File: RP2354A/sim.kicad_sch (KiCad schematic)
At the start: 10 parts

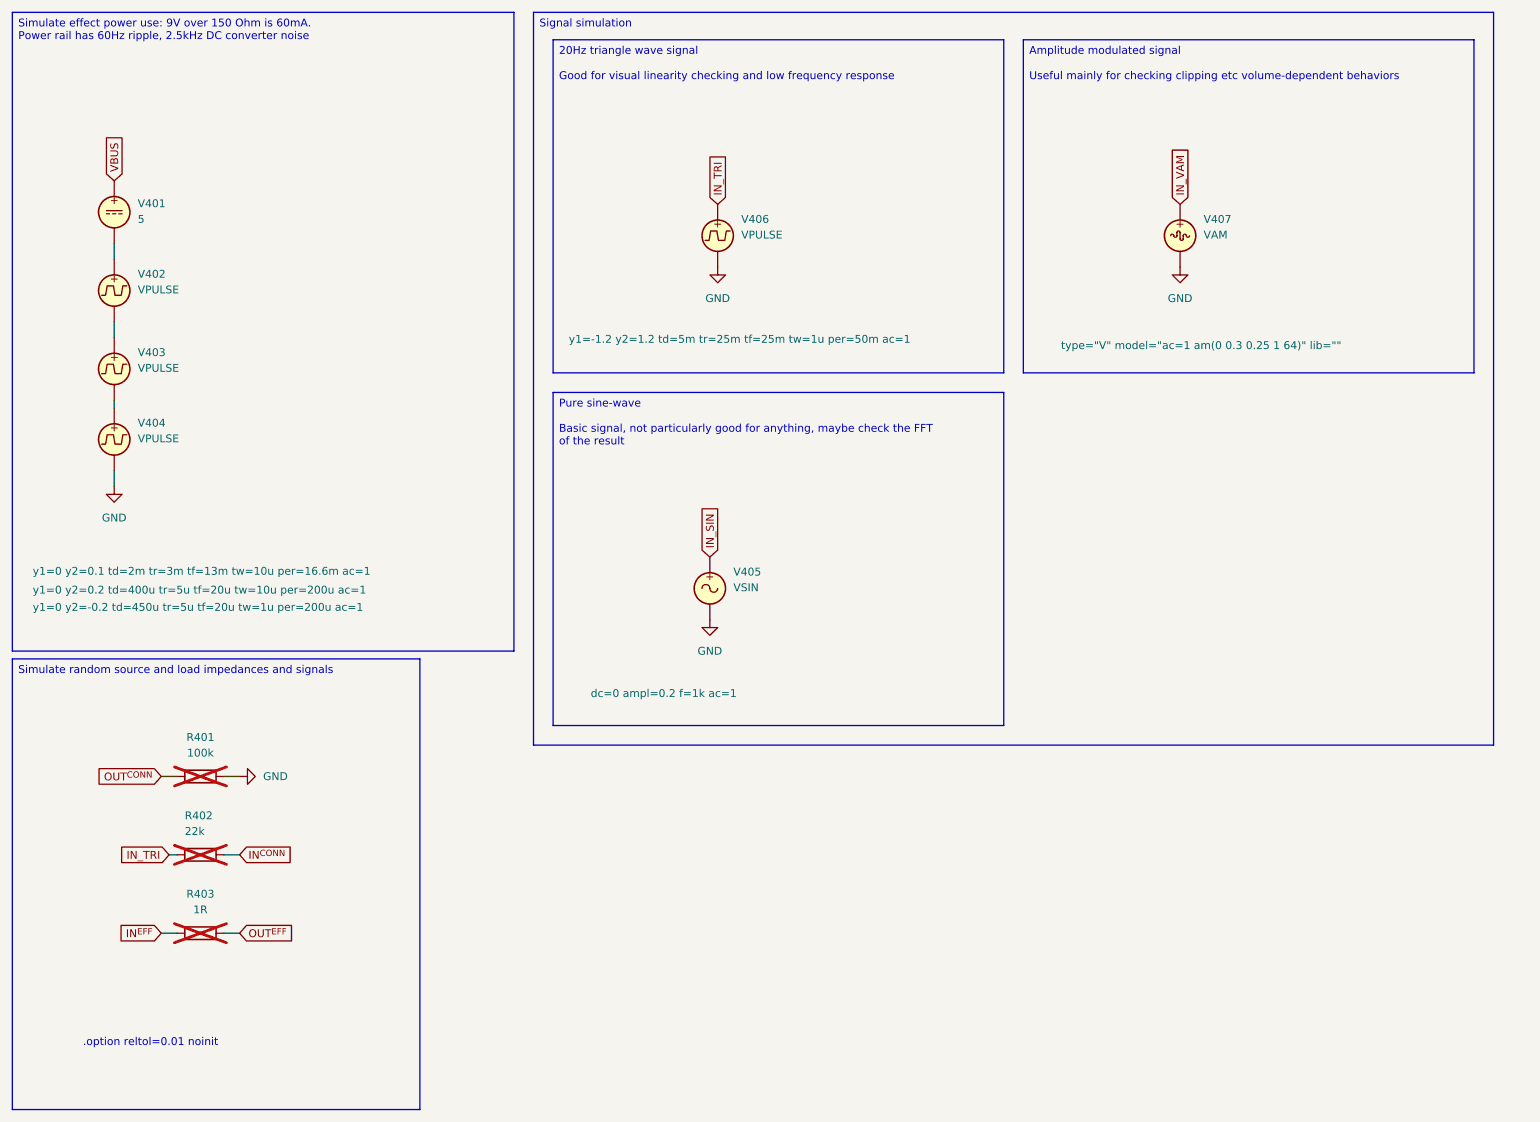
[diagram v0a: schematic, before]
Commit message: Switch the MMBF5103 JFET over to a OPA365 op amp
This is a long time coming, but it was triggered by jlcpcb not stocking
the MMBF5103, and all the alternatives looked worse.  So I guess sanity
has to prevail, and I should use an opamp rather than a discrete JFET
input stage.

I looked at the J201 - which I have tested and works, but has a
potentially very low V_{GSOFF} that will cause clipping.  And the
MMBFJ309L looked good in simulation and had better parameter values, but
I've never tested it, so it seemed a bit risky particularly since the
intended market seems to be for much higher frequency circuits.

I even looked at the JFE150, which is another silly-expensive thing sold
to audio markets.  I guess that tracks.

In the end, a plain simple opamp is definitely the sane choice.

To rebias the incoming signal, this uses the MICBIAS from the TAC5112,
which is typically 2.75V (but can be programmed to 2.5V or turned off
entirely etc).  It's there, it's almost what it is meant for, so let's
use it.

The OPA365 looks fine, and does rail-to-rail input and output and can do
single supplies down to 2.2V, but rather than put even more on the 3.3V
rail (and limiting the voltage swing), this just uses the 5V USB VBUS
power supply.

This does have some minimal caps for filtering (replacing the old +VA
supply to the JFET) but the OPA365 also claims good PSRR.

This all does seem like the right thing to do, but I'm still a bit sad
since the discrete JFET was just more interesting.

Signed-off-by: Linus Torvalds <torvalds@linux-foundation.org>
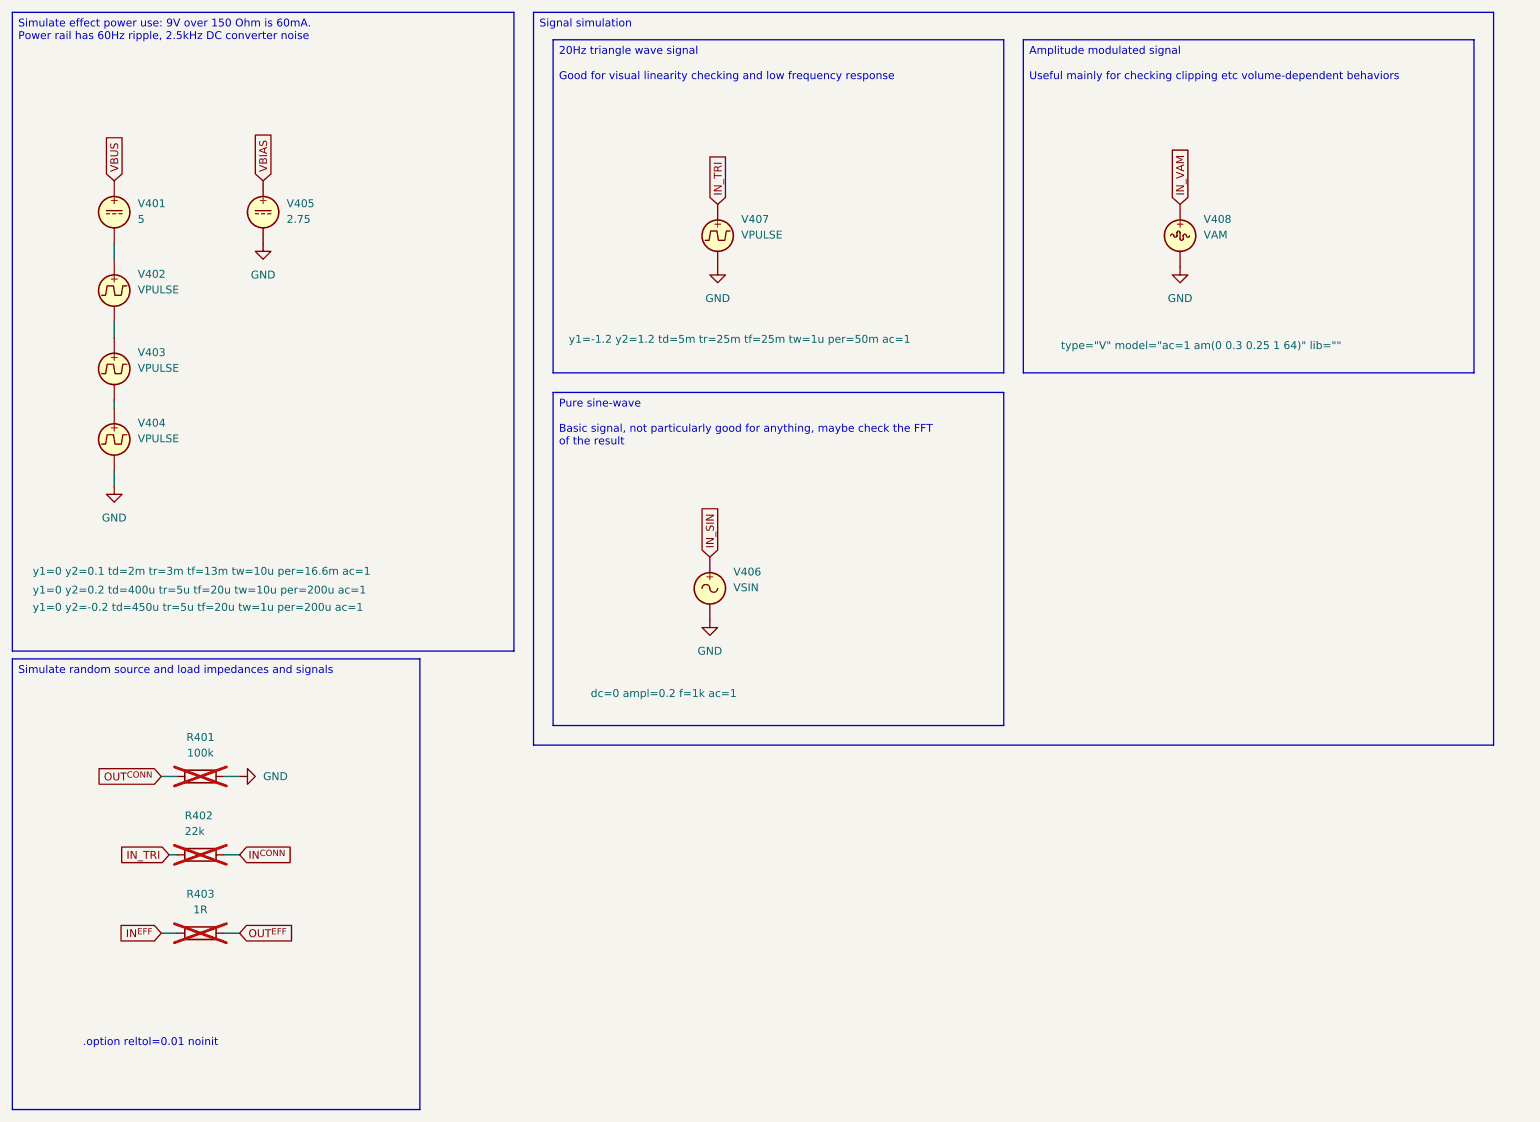
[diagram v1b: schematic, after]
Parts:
- added V405: 2.75, symbol Simulation_SPICE:VDC
- renumbered V405 to V406, V406 to V407, V407 to V408
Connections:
- net GND: now also V405.2
- new net VBIAS: V405.1
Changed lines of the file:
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@@
+		)
+	)
+	(global_label "VBIAS"
+		(shape input)
+		(at 54.61 41.91 90)
+		(fields_autoplaced yes)
+		(effects
+			(font
+				(size 1.27 1.27)
+			)
+			(justify left)
+		)
+		(property "Intersheetrefs" "${INTERSHEET_REFS}"
+			(at 54.61 33.6633 90)
+			(effects
+				(font
+					(size 1.27 1.27)
+				)
+				(justify left)
+				(hide yes)
+			)
 		)
 	)
@@
 		(dnp no)
 		(fields_autoplaced yes)
-		(property "Reference" "#PWR0303"
+		(property "Reference" "#PWR0404"
 			(at 127 119.38 0)
 			(effects
@@
 			(project "Stomp"
 				(path "/9e337e0b-885b-4d2b-99a2-62cdd082c615/a1084b87-85fd-4b63-8fe4-8749c999d338"
-					(reference "#PWR0303")
+					(reference "#PWR0404")
 					(unit 1)
 				)
@@
 		(on_board no)
 		(dnp no)
-		(property "Reference" "V405"
+		(property "Reference" "V406"
 			(at 130.81 105.2801 0)
 			(effects
@@
 			(project "Stomp"
 				(path "/9e337e0b-885b-4d2b-99a2-62cdd082c615/a1084b87-85fd-4b63-8fe4-8749c999d338"
-					(reference "V405")
+					(reference "V406")
 					(unit 1)
 				)
@@
 		(on_board no)
 		(dnp no)
-		(property "Reference" "V407"
+		(property "Reference" "V408"
 			(at 207.01 48.1301 0)
 			(effects
@@
 			(project "Stomp"
 				(path "/9e337e0b-885b-4d2b-99a2-62cdd082c615/a1084b87-85fd-4b63-8fe4-8749c999d338"
-					(reference "V407")
+					(reference "V408")
 					(unit 1)
 				)
@@
 				(path "/9e337e0b-885b-4d2b-99a2-62cdd082c615/a1084b87-85fd-4b63-8fe4-8749c999d338"
 					(reference "R401")
+					(unit 1)
+				)
+			)
+		)
+	)
+	(symbol
+		(lib_id "Simulation_SPICE:VDC")
+		(at 54.61 46.99 0)
+		(unit 1)
+		(exclude_from_sim no)
+		(in_bom no)
+		(on_board no)
+		(dnp no)
+		(fields_autoplaced yes)
+		(property "Reference" "V405"
+			(at 58.42 45.5901 0)
+			(effects
+				(font
+					(size 1.27 1.27)
+				)
+				(justify left)
+			)
+		)
+		(property "Value" "2.75"
+			(at 58.42 48.1301 0)
+			(effects
+				(font
+					(size 1.27 1.27)
+				)
+				(justify left)
+			)
+		)
+		(property "Footprint" ""
+			(at 54.61 46.99 0)
+			(effects
+				(font
+					(size 1.27 1.27)
+				)
+				(hide yes)
+			)
+		)
+		(property "Datasheet" "https://ngspice.sourceforge.io/docs/ngspice-html-manual/manual.xhtml#sec_Independent_Sources_for"
+			(at 54.61 46.99 0)
+			(effects
+				(font
+					(size 1.27 1.27)
+				)
+				(hide yes)
+			)
+		)
+		(property "Description" "Voltage source, DC"
+			(at 54.61 46.99 0)
+			(effects
+				(font
+					(size 1.27 1.27)
+				)
+				(hide yes)
+			)
+		)
+		(property "Sim.Pins" "1=+ 2=-"
+			(at 54.61 46.99 0)
+			(effects
+				(font
+					(size 1.27 1.27)
+				)
+				(hide yes)
+			)
+		)
+		(property "Sim.Type" "DC"
+			(at 54.61 46.99 0)
+			(effects
+				(font
+					(size 1.27 1.27)
+				)
+				(hide yes)
+			)
+		)
+		(property "Sim.Device" "V"
+			(at 54.61 46.99 0)
+			(effects
+				(font
+					(size 1.27 1.27)
+				)
+				(justify left)
+				(hide yes)
+			)
+		)
+		(pin "1"
+		)
+		(pin "2"
+		)
+		(instances
+			(project "RP2354A"
+				(path "/9e337e0b-885b-4d2b-99a2-62cdd082c615/a1084b87-85fd-4b63-8fe4-8749c999d338"
+					(reference "V405")
 					(unit 1)
 				)
@@
 		(dnp no)
 		(fields_autoplaced yes)
-		(property "Reference" "#PWR0306"
+		(property "Reference" "#PWR0402"
 			(at 57.15 138.43 0)
 			(effects
@@
 			(project "Stomp"
 				(path "/9e337e0b-885b-4d2b-99a2-62cdd082c615/a1084b87-85fd-4b63-8fe4-8749c999d338"
-					(reference "#PWR0306")
+					(reference "#PWR0402")
 					(unit 1)
 				)
@@
 		(dnp no)
 		(fields_autoplaced yes)
-		(property "Reference" "#PWR0301"
+		(property "Reference" "#PWR0401"
 			(at 30.48 97.79 0)
 			(effects
@@
 			(project "Stomp"
 				(path "/9e337e0b-885b-4d2b-99a2-62cdd082c615/a1084b87-85fd-4b63-8fe4-8749c999d338"
-					(reference "#PWR0301")
+					(reference "#PWR0401")
 					(unit 1)
 				)
@@
 		(on_board no)
 		(dnp no)
-		(property "Reference" "V406"
+		(property "Reference" "V407"
 			(at 132.08 48.1301 0)
 			(effects
@@
 			(project "Stomp"
 				(path "/9e337e0b-885b-4d2b-99a2-62cdd082c615/a1084b87-85fd-4b63-8fe4-8749c999d338"
-					(reference "V406")
+					(reference "V407")
 					(unit 1)
 				)
@@
 		(dnp no)
 		(fields_autoplaced yes)
-		(property "Reference" "#PWR0304"
+		(property "Reference" "#PWR0405"
 			(at 128.27 62.23 0)
 			(effects
@@
 			(project "Stomp"
 				(path "/9e337e0b-885b-4d2b-99a2-62cdd082c615/a1084b87-85fd-4b63-8fe4-8749c999d338"
-					(reference "#PWR0304")
+					(reference "#PWR0405")
 					(unit 1)
 				)
@@
 				(path "/9e337e0b-885b-4d2b-99a2-62cdd082c615/a1084b87-85fd-4b63-8fe4-8749c999d338"
 					(reference "V401")
+					(unit 1)
+				)
+			)
+		)
+	)
+	(symbol
+		(lib_id "power:GND")
+		(at 54.61 52.07 0)
+		(unit 1)
+		(exclude_from_sim no)
+		(in_bom yes)
+		(on_board yes)
+		(dnp no)
+		(fields_autoplaced yes)
+		(property "Reference" "#PWR0403"
+			(at 54.61 58.42 0)
+			(effects
+				(font
+					(size 1.27 1.27)
+				)
+				(hide yes)
+			)
+		)
+		(property "Value" "GND"
+			(at 54.61 57.15 0)
+			(effects
+				(font
+					(size 1.27 1.27)
+				)
+			)
+		)
+		(property "Footprint" ""
+			(at 54.61 52.07 0)
+			(effects
+				(font
+					(size 1.27 1.27)
+				)
+				(hide yes)
+			)
+		)
+		(property "Datasheet" ""
+			(at 54.61 52.07 0)
+			(effects
+				(font
+					(size 1.27 1.27)
+				)
+				(hide yes)
+			)
+		)
+		(property "Description" "Power symbol creates a global label with name \"GND\" , ground"
+			(at 54.61 52.07 0)
+			(effects
+				(font
+					(size 1.27 1.27)
+				)
+				(hide yes)
+			)
+		)
+		(pin "1"
+		)
+		(instances
+			(project "RP2354A"
+				(path "/9e337e0b-885b-4d2b-99a2-62cdd082c615/a1084b87-85fd-4b63-8fe4-8749c999d338"
+					(reference "#PWR0403")
 					(unit 1)
 				)
@@
 		(dnp no)
 		(fields_autoplaced yes)
-		(property "Reference" "#PWR0307"
+		(property "Reference" "#PWR0406"
 			(at 203.2 62.23 0)
 			(effects
@@
 			(project "Stomp"
 				(path "/9e337e0b-885b-4d2b-99a2-62cdd082c615/a1084b87-85fd-4b63-8fe4-8749c999d338"
-					(reference "#PWR0307")
+					(reference "#PWR0406")
 					(unit 1)
 				)
